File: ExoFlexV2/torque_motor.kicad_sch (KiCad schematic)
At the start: 35 parts, among them U21 SN74HC7032D_V2, U28 ADCMP602BRMZ, U29 ADCMP602BRMZ, U30 ADCMP602BRMZ, U31 SN74LVC3G14DCUT_V2, U32 SN74LV4T08PWR_V2, U33 SN74HC7032D_V2

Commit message: quque truc
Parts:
- removed R37, R38, R39: R_Small_US, Resistor_SMD:R_0603_1608Metric, symbol Device:R_Small_US
- removed TP16, TP17, TP18: 5005, FootPrint:KEYSTONE_5005, symbol SymLib:5005
- added C86, C87, C88, C89, C90, C91: 1nF, Capacitor_SMD:C_0603_1608Metric, symbol Device:C
- added R69, R70, R71: 0 ohm, Resistor_SMD:R_0603_1608Metric, symbol Device:R_Small_US
- added R74, R75, R76, R77, R78, R79: 7,5k, Resistor_SMD:R_0603_1608Metric, symbol Device:R_Small_US
- added TP42, TP43, TP44, TP45, TP46, TP47, TP51: 5005, FootPrint:KEYSTONE_5005, symbol SymLib:5005
- renumbered C73 to C100, C74 to C101, C75 to C102, C76 to C103, C77 to C104, C65 to C92, C66 to C93, C67 to C94, C68 to C95, C69 to C96, C70 to C97, C71 to C98, C72 to C99, R31 to R65, R32 to R66, R33 to R67, R34 to R68, R35 to R72, R36 to R73, TP19 to TP48, TP20 to TP49, TP21 to TP50, U21 to U20, U28 to U30, U29 to U31, U30 to U32, U31 to U33, U32 to U34, U33 to U35
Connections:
- net +5V: no longer R65.1, R67.1, R72.1
- net +5VA: now also R65.1, R67.1, R72.1; no longer C100.2, C101.2, C102.2, C103.2, C104.2, C92.2, C93.2, C94.2, C95.2, C96.2, C97.2, C98.2, C99.2, R66.1, R68.1, R73.1, U30.6 (GND), U31.6 (GND), U32.6 (GND), U33.7 (GND), U35.7 (GND)
- net LC1_POT_OUT: now also R75.1; no longer U30.3 (VN)
- net LC2_POT_OUT: now also R76.1; no longer U31.3 (VN)
- net LC3_POT_OUT: now also R79.1; no longer U32.3 (VN)
- net TOR_MOT_1: now also C90.1, R78.2
- net TOR_MOT_2: now also C86.1, R74.2
- net TOR_MOT_3: now also C89.1, R77.2
- net TOR_MOT_SEC: now also TP51.TP
- new net: R69.1, TP42.TP
- new net: R71.1, TP44.TP
- new net: R70.1, TP43.TP
- new net GND: C100.2, C101.2, C102.2, C103.2, C104.2, C86.2, C87.2, C88.2, C89.2, C90.2, C91.2, C92.2, C93.2, C94.2, C95.2, C96.2, C97.2, C98.2, C99.2, R66.1, R68.1, R73.1, U30.6 (GND), U31.6 (GND), U32.6 (GND), U33.7 (GND), U35.7 (GND)
- new net LC_LIM_1: C87.1, R75.2, TP45.TP, U30.3 (VN)
- new net LC_LIM_2: C88.1, R76.2, TP46.TP, U31.3 (VN)
- new net LC_LIM_3: C91.1, R79.2, TP47.TP, U32.3 (VN)
- new net TOR_MOT_OUT_1: R69.2, R78.1
- new net TOR_MOT_OUT_2: R70.2, R74.1
- new net TOR_MOT_OUT_3: R71.2, R77.1

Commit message: Placement
Début du placement et modification d'après dernier review
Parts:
- removed R65, R66, R67, R68, R72, R73: R_Small_US, Resistor_SMD:R_0603_1608Metric, symbol Device:R_Small_US
- added TP76, TP78, TP80, TP85, TP86, TP87: 5005, FootPrint:KEYSTONE_5005, symbol SymLib:5005
- R64: renamed from R69; value 0 ohm -> 0Ω
- R65: renamed from R70; value 0 ohm -> 0Ω
- R66: renamed from R71; value 0 ohm -> 0Ω
- renumbered C96 to C100, C97 to C101, C98 to C102, C99 to C103, C100 to C104, C101 to C105, C102 to C106, C103 to C107, C104 to C108, C87 to C91, C86 to C92, C88 to C93, C89 to C94, C91 to C95, C92 to C96, C93 to C97, C94 to C98, C95 to C99, R78 to R67, R75 to R68, R74 to R69, R76 to R70, R77 to R71, R79 to R72, TP42 to TP73, TP43 to TP74, TP44 to TP75, TP45 to TP77, TP46 to TP79, TP47 to TP81, TP48 to TP82, TP49 to TP83, TP50 to TP84, TP51 to TP88
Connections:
- net TOR_MOT_1: now also TP76.TP
- net TOR_MOT_2: now also TP78.TP
- net TOR_MOT_3: now also TP80.TP
- net at U20.11 (4Y), U35.1 (1A): now also TP86.TP
- net at U34.8 (3Y), U35.2 (1B): now also TP87.TP
- net at U33.7 (GND), U34.9 (3A): now also TP85.TP
- net LC_LIM_1: no longer names the net of C91.1, R68.2, TP77.TP, U30.3 (VN)
- net LC_LIM_2: no longer names the net of C93.1, R70.2, TP79.TP, U31.3 (VN)
- net LC_LIM_3: no longer names the net of C95.1, R72.2, TP81.TP, U32.3 (VN)
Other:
- moved on the sheet: C90, C91, C92, C93, C94, C95, R67, R68, R69, R70, R71, R72

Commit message: Placement encore
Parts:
- renumbered C99 to C100, C100 to C101, C101 to C102, C102 to C103, C103 to C104, C104 to C105, C105 to C106, C106 to C107, C107 to C108, C108 to C109, C90 to C91, C91 to C92, C92 to C93, C93 to C94, C94 to C95, C95 to C96, C96 to C97, C97 to C98, C98 to C99, R64 to R65, R65 to R66, R66 to R67, R67 to R68, R68 to R69, R69 to R70, R70 to R71, R71 to R72, R72 to R73

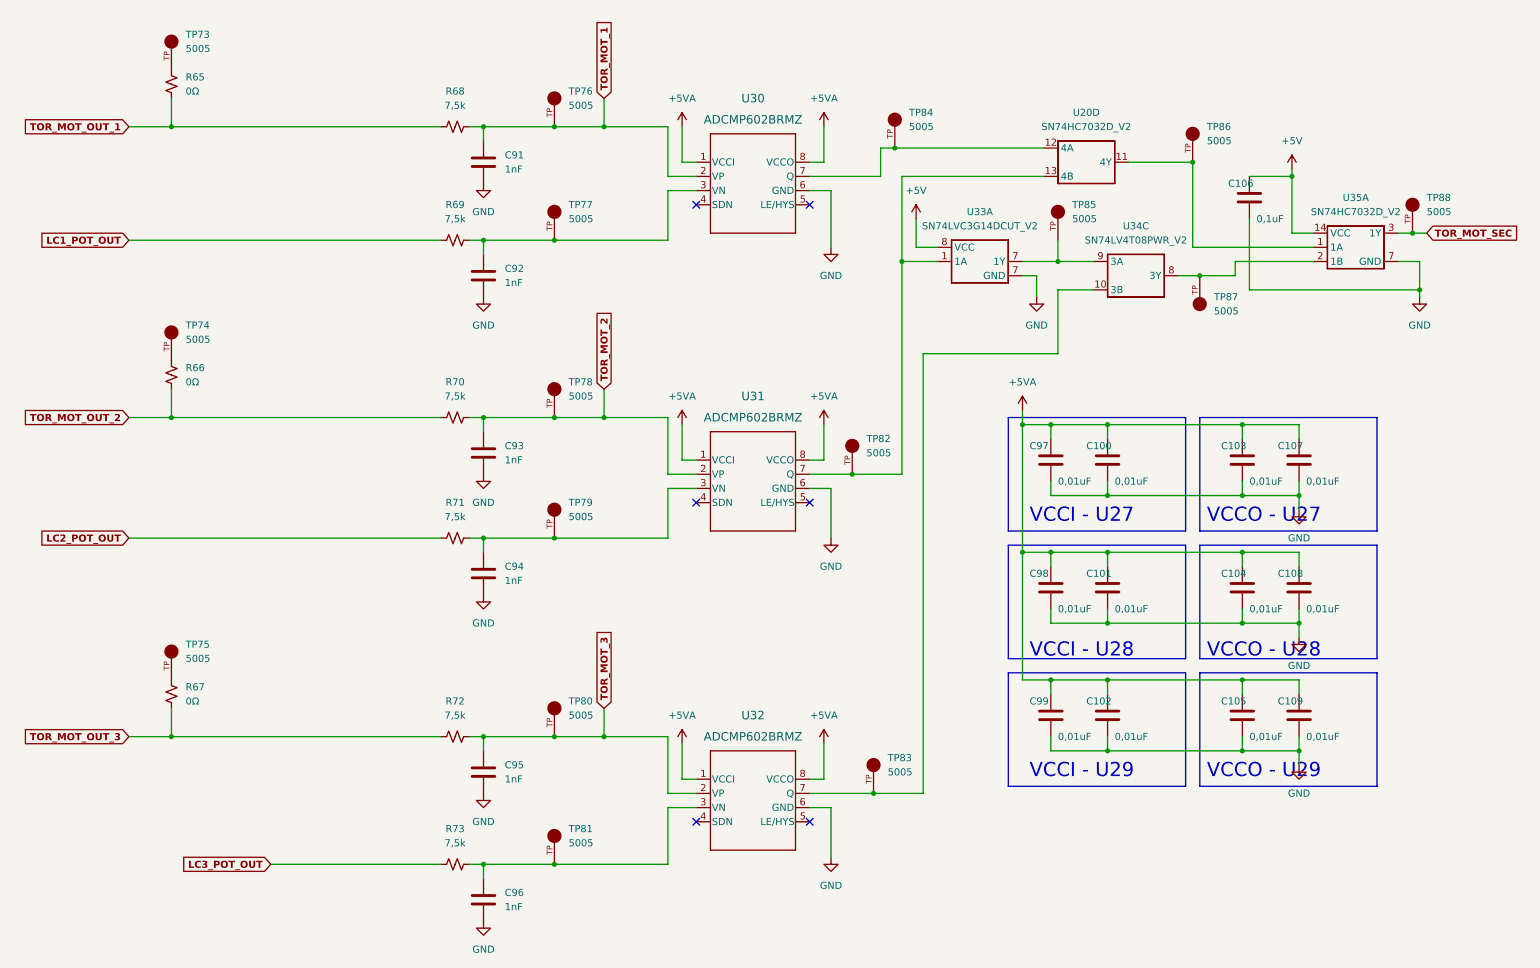
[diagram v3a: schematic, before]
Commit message: Mise à jour mi-stage
- Torque et Amplitude testé et vérifié
- Capteur de présence et de proximité testé
- Système de détection de coupure de fils
- Polyvalence pour plusieurs capteurs
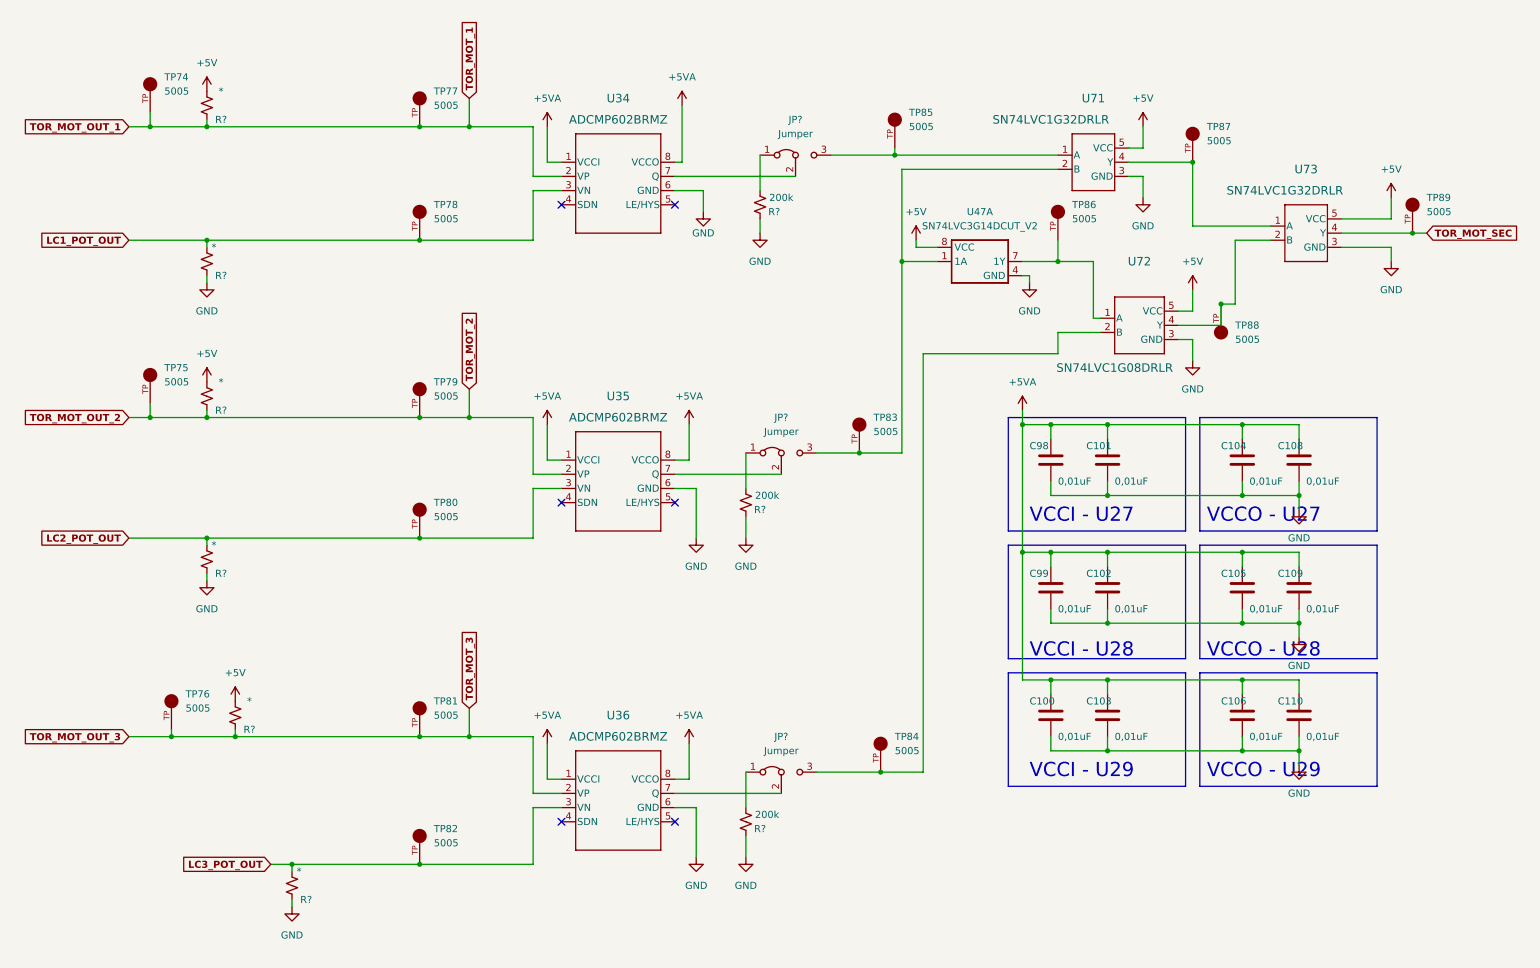
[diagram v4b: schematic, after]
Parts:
- removed C106: 0,1uF, Capacitor_SMD:C_0603_1608Metric, symbol Device:C
- removed C91, C92, C93, C94, C95, C96: 1nF, Capacitor_SMD:C_0603_1608Metric, symbol Device:C
- removed R65, R66, R67: 0Ω, Resistor_SMD:R_0603_1608Metric, symbol Device:R_Small_US
- removed R68, R69, R70, R71, R72, R73: 7,5k, Resistor_SMD:R_0603_1608Metric, symbol Device:R_Small_US
- removed U20, U35: SN74HC7032D_V2, FootPrint:SN74HC7032D, symbol SymLib:SN74HC7032D_V2
- removed U33: SN74LVC3G14DCUT_V2, FootPrint:SN74LVC3G14DCUT, symbol SymLib:SN74LVC3G14DCUT_V2
- removed U34: SN74LV4T08PWR_V2, FootPrint:SN74LV4T08PWR, symbol SymLib:SN74LV4T08PWR_V2
- added JP? (x3): Jumper, Connector_PinHeader_2.54mm:PinHeader_1x03_P2.54mm_Vertical, symbol Jumper:Jumper_3_Bridged12
- added R? (x3): 200k, Resistor_SMD:R_0603_1608Metric, symbol Device:R_Small_US
- added R? (x6): *, Resistor_SMD:R_0603_1608Metric, symbol Device:R_Small_US
- added U47: SN74LVC3G14DCUT_V2, FootPrint:SN74LVC3G14DCUT, symbol SymLib:SN74LVC3G14DCUT_V2
- added U71, U73: SN74LVC1G32DRLR, FootPrint:DRL5, symbol SymLib:SN74LVC1G32DRLR
- added U72: SN74LVC1G08DRLR, FootPrint:DRL5, symbol SymLib:SN74LVC1G08DRLR
- renumbered C99 to C100, C100 to C101, C101 to C102, C102 to C103, C103 to C104, C104 to C105, C105 to C106, C107 to C108, C108 to C109, C109 to C110, C97 to C98, C98 to C99, TP73 to TP74, TP74 to TP75, TP75 to TP76, TP76 to TP77, TP77 to TP78, TP78 to TP79, TP79 to TP80, TP80 to TP81, TP81 to TP82, TP82 to TP83, TP83 to TP84, TP84 to TP85, TP85 to TP86, TP86 to TP87, TP87 to TP88, TP88 to TP89, U30 to U34, U31 to U35, U32 to U36
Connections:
- net +5V: now also R?.1, R?.1, R?.1, U47.8 (VCC), U71.5 (VCC), U72.5 (VCC), U73.5 (VCC)
- net GND: now also R?.2, R?.2, R?.2, R?.2, R?.2, R?.2, U47.4 (GND), U71.3 (GND), U72.3 (GND), U73.3 (GND)
- net LC1_POT_OUT: now also TP78.TP, U34.3 (VN), R?.1
- net LC2_POT_OUT: now also TP80.TP, U35.3 (VN), R?.1
- net LC3_POT_OUT: now also TP82.TP, U36.3 (VN), R?.1
- net TOR_MOT_1: now also TP74.TP, R?.2
- net TOR_MOT_2: now also TP75.TP, R?.2
- net TOR_MOT_3: now also TP76.TP, R?.2
- net TOR_MOT_SEC: now also U73.4 (Y)
- net at TP87.TP: now also U71.4 (Y), U73.1 (A)
- net at TP88.TP: now also U72.4 (Y), U73.2 (B)
- net at U35.7 (Q): now also JP?.2 (C); no longer TP83.TP
- net at TP86.TP: now also U47.7 (1Y), U72.1 (A)
- net at TP85.TP: now also JP?.3 (B), U71.1 (A); no longer U34.7 (Q)
- net at U36.7 (Q): now also JP?.2 (C); no longer TP84.TP
- new net: JP?.1 (A), R?.1 (x3)
- new net: JP?.3 (B), TP84.TP, U72.2 (B)
- new net: JP?.3 (B), TP83.TP, U47.1 (1A), U71.2 (B)
- new net: JP?.2 (C), U34.7 (Q)
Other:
- moved on the sheet: TP74, TP75, TP76, TP77, TP78, TP79, TP80, TP81, TP82, TP83, TP84, TP88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
